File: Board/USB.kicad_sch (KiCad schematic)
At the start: 29 parts, among them IC8 MAX3421E, Q2 32kHz, Q3 12MHz

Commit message: preview for r1.3
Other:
- note added: "CBM-ULTIPET-V1.3A"
- note removed: "CBM-ULTIPET-V1.2A"
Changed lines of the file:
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@@
 	(generator_version "9.0")
 	(paper "User" 357.683 261.772)
-	(text "CBM-ULTIPET-V1.2A"
+	(text "CBM-ULTIPET-V1.3A"
 		(exclude_from_sim no)
 		(at 231.14 210.82 0)

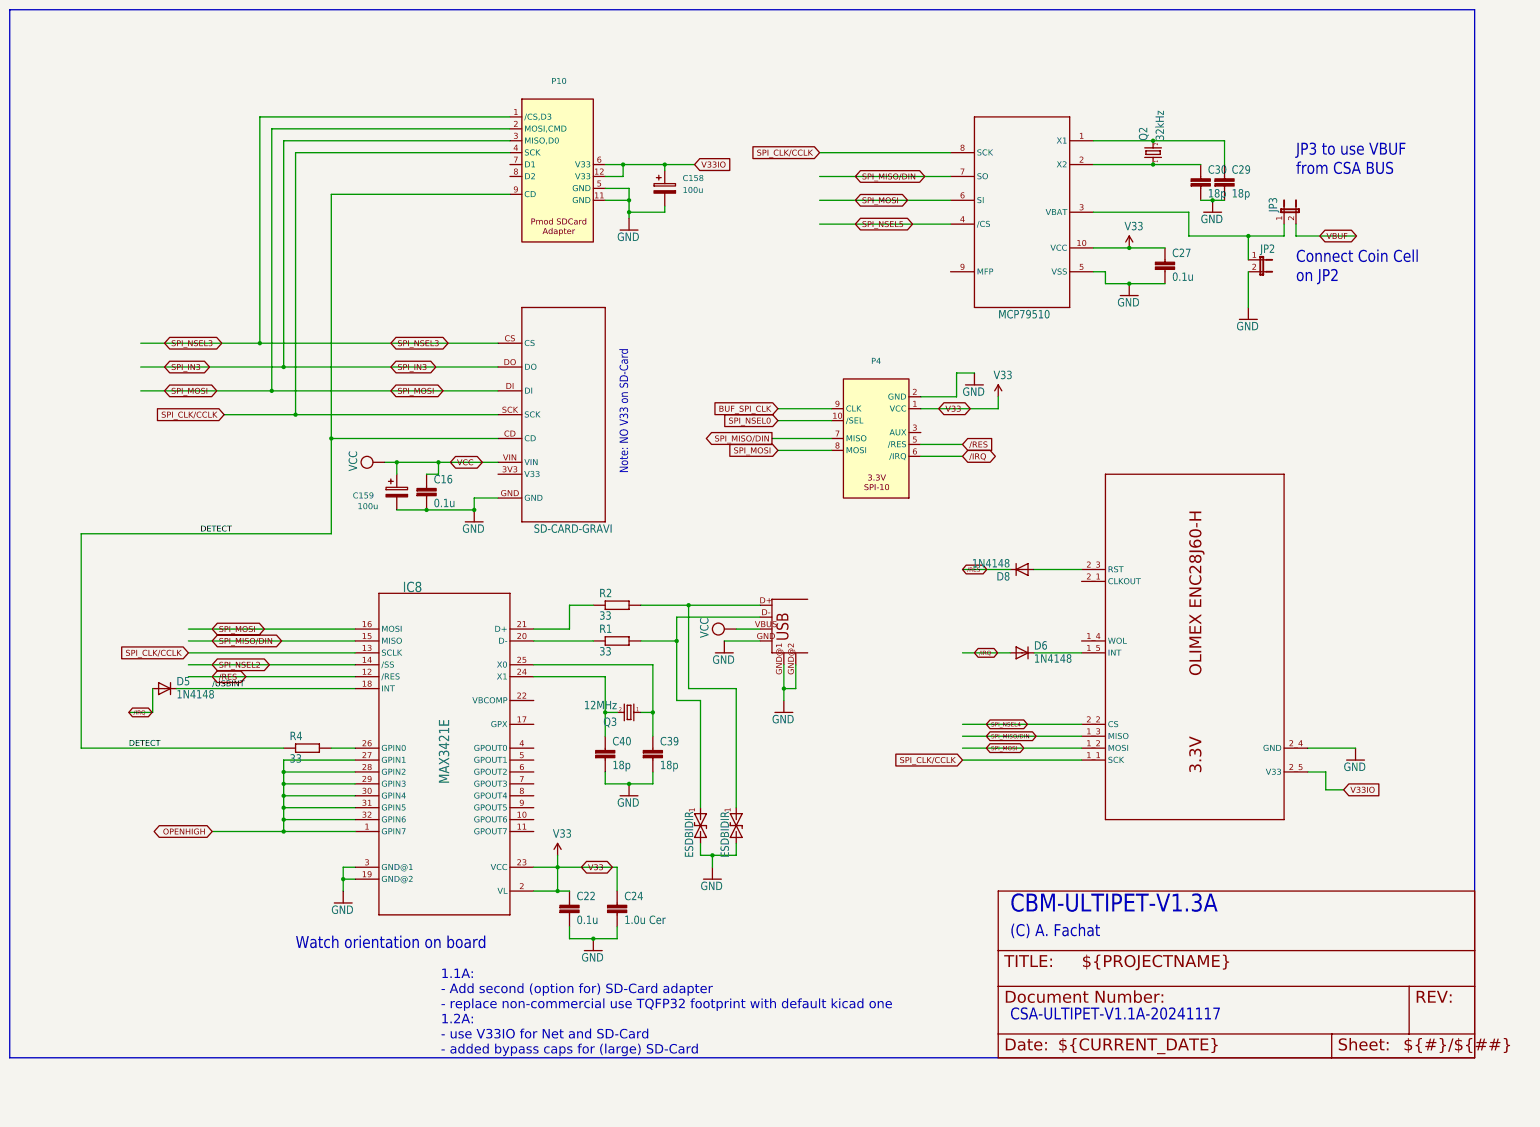
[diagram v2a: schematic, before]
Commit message: add some jumper options, layout work
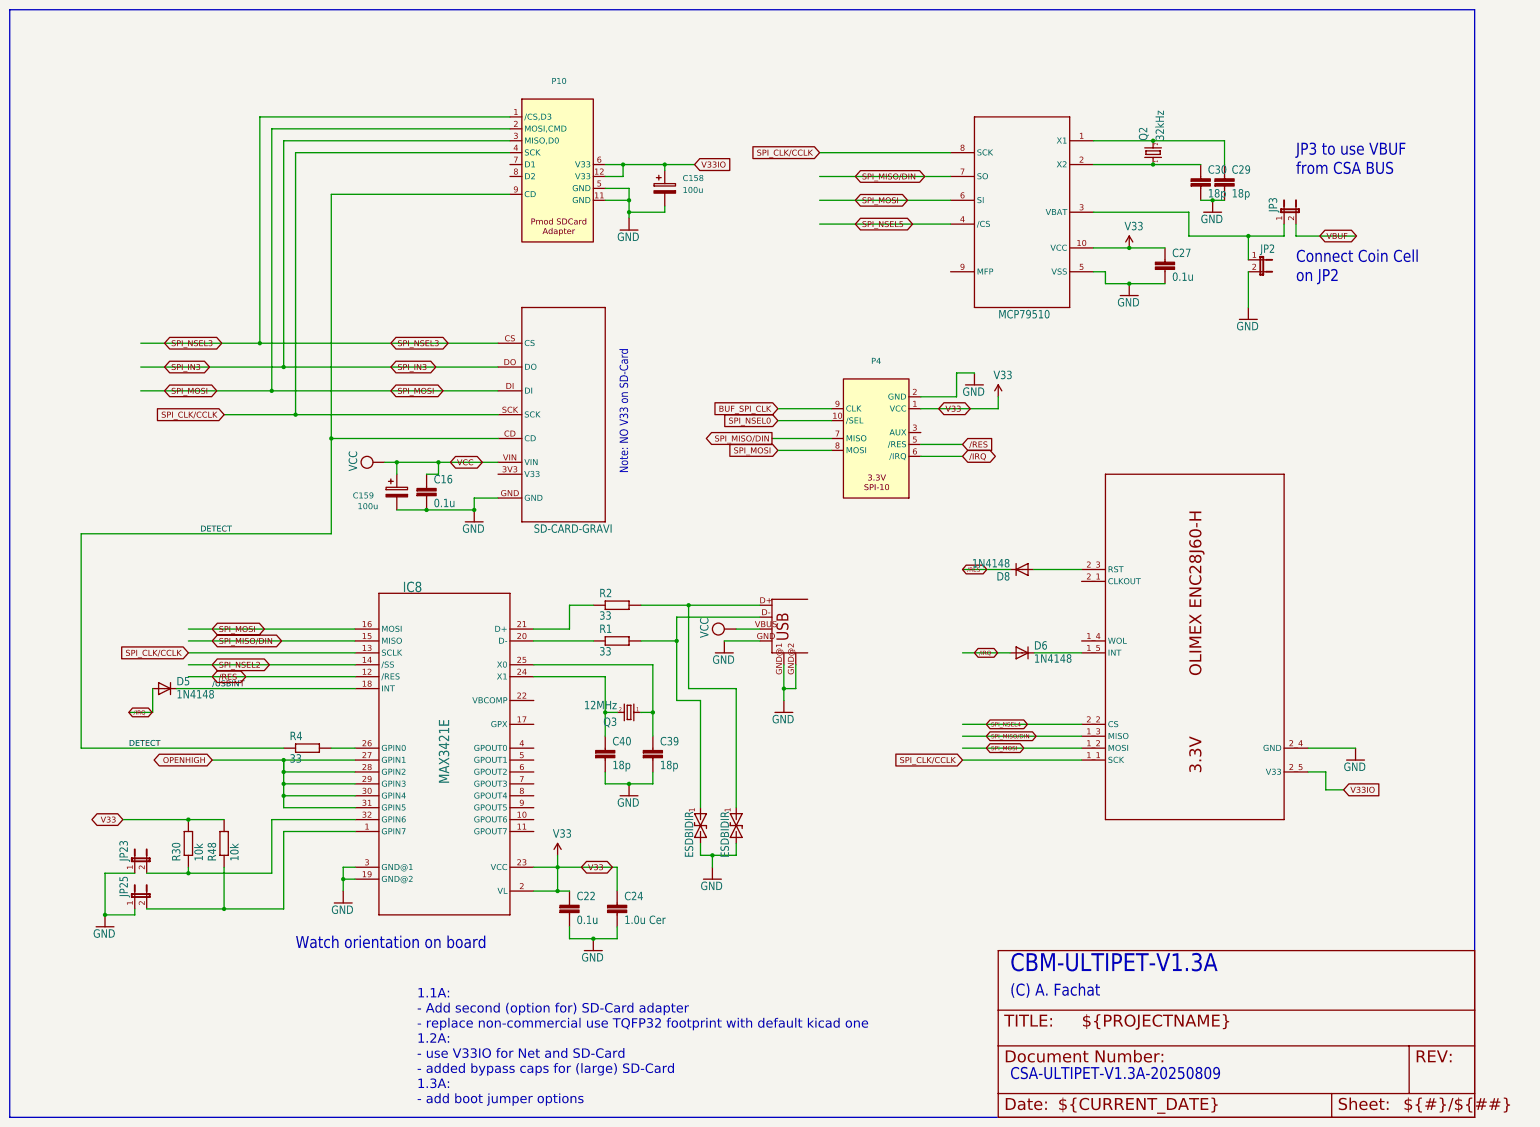
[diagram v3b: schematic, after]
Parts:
- added JP23, JP25: JP1E, cbm_ultipet_v1:JP1, symbol csa_ultracpu-eagle-import:JP1E
- added R30, R48: 10k, Resistor_SMD:R_0805_2012Metric_Pad1.20x1.40mm_HandSolder, symbol csa_ultracpu-eagle-import:R-EU_0204/7
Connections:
- net GND: now also JP23.1, JP25.1
- net OPENHIGH: no longer IC8.1 (GPIN7), IC8.32 (GPIN6)
- net V33: now also R30.2, R48.2
- new net: IC8.1 (GPIN7), JP25.2, R48.1
- new net: IC8.32 (GPIN6), JP23.2, R30.1
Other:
- note added: "1.1A: - Add second (option for) SD-Card adapter - replace non-commercial use TQFP32 footprint with default kicad one 1.2A: - use V33IO for Net and SD-Card - added bypass caps for (large) SD-Card 1.3A: - add boot jumper options"
- note added: "CSA-ULTIPET-V1.3A-20250809"
- note removed: "1.1A: - Add second (option for) SD-Card adapter - replace non-commercial use TQFP32 footprint with default kicad one 1.2A: - use V33IO for Net and SD-Card - added bypass caps for (large) SD-Card"
- note removed: "CSA-ULTIPET-V1.1A-20241117"

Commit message: rename U refs to UX*
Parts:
- renumbered U$12 to UX12, U$13 to UX13, U$14 to UX14, U$15 to UX15, U$9 to UX9
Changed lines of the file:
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@@
 		(on_board yes)
 		(dnp no)
-		(property "Reference" "U$13"
+		(property "Reference" "UX13"
 			(at 228.6 40.64 0)
 			(effects
@@
 			(project "cbm_ultipet_v1"
 				(path "/4dd2dd78-173f-4b46-8cce-4ed940435c94/d2c8cba7-54fd-4ca0-bac7-9d690d7d8e89"
-					(reference "U$13")
+					(reference "UX13")
 					(unit 1)
 				)
@@
 		(on_board yes)
 		(dnp no)
-		(property "Reference" "U$9"
+		(property "Reference" "UX9"
 			(at 281.94 190.5 0)
 			(effects
@@
 			(project "cbm_ultipet_v1"
 				(path "/4dd2dd78-173f-4b46-8cce-4ed940435c94/d2c8cba7-54fd-4ca0-bac7-9d690d7d8e89"
-					(reference "U$9")
+					(reference "UX9")
 					(unit 1)
 				)
@@
 		(on_board yes)
 		(dnp no)
-		(property "Reference" "U$15"
+		(property "Reference" "UX15"
 			(at 167.005 188.722 0)
 			(effects
@@
 			(project "cbm_ultipet_v1"
 				(path "/4dd2dd78-173f-4b46-8cce-4ed940435c94/d2c8cba7-54fd-4ca0-bac7-9d690d7d8e89"
-					(reference "U$15")
+					(reference "UX15")
 					(unit 1)
 				)
@@
 		(on_board yes)
 		(dnp no)
-		(property "Reference" "U$14"
+		(property "Reference" "UX14"
 			(at 174.625 188.722 0)
 			(effects
@@
 			(project "cbm_ultipet_v1"
 				(path "/4dd2dd78-173f-4b46-8cce-4ed940435c94/d2c8cba7-54fd-4ca0-bac7-9d690d7d8e89"
-					(reference "U$14")
+					(reference "UX14")
 					(unit 1)
 				)
@@
 		(on_board yes)
 		(dnp no)
-		(property "Reference" "U$12"
+		(property "Reference" "UX12"
 			(at 129.54 81.28 0)
 			(effects
@@
 			(project "cbm_ultipet_v1"
 				(path "/4dd2dd78-173f-4b46-8cce-4ed940435c94/d2c8cba7-54fd-4ca0-bac7-9d690d7d8e89"
-					(reference "U$12")
-					(unit 1)
-				)
+					(reference "UX12")
+					(unit 1)
+				)

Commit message: some layout fixes, more parts
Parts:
- C158, C159: footprint Capacitor_THT:CP_Radial_D5.0mm_P2.50mm -> Capacitor_THT:CP_Radial_D5.0mm_P2.00mm
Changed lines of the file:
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@@
 			)
 		)
-		(property "Footprint" "Capacitor_THT:CP_Radial_D5.0mm_P2.50mm"
+		(property "Footprint" "Capacitor_THT:CP_Radial_D5.0mm_P2.00mm"
 			(at 158.4452 59.69 0)
 			(effects
@@
 			)
 		)
-		(property "Footprint" "Capacitor_THT:CP_Radial_D5.0mm_P2.50mm"
+		(property "Footprint" "Capacitor_THT:CP_Radial_D5.0mm_P2.00mm"
 			(at 101.2952 124.46 0)
 			(effects
